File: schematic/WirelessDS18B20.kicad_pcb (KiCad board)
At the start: 2 copper layers, 25.4 x 30.5 mm, 14 parts, among them P1 Power Connector, P2 1-Wire Bus, P3 SERIAL_TX, Q1 BS170, SW1 RESCUE_MODE, SW2 RESET, U1 AMS1117 3.3, U2 ESP-01

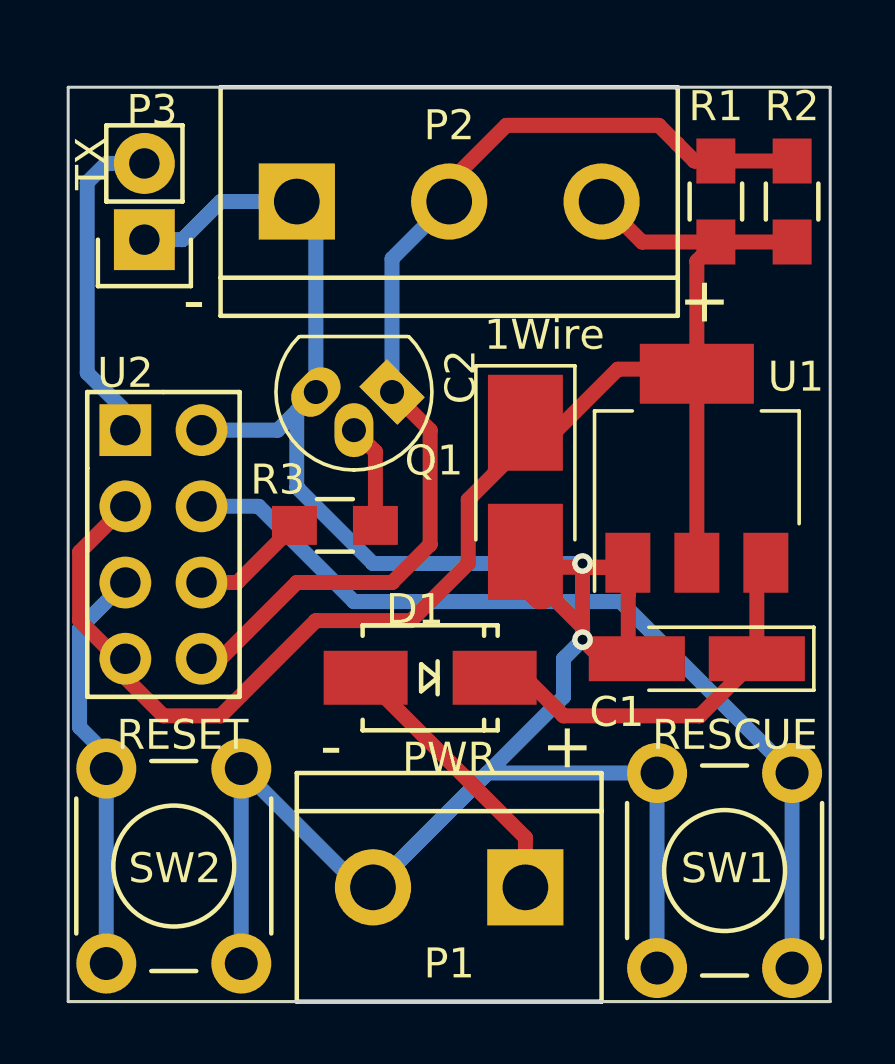
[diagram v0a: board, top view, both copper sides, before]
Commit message: Improve Schematic (update KiCad to 4.0.7)
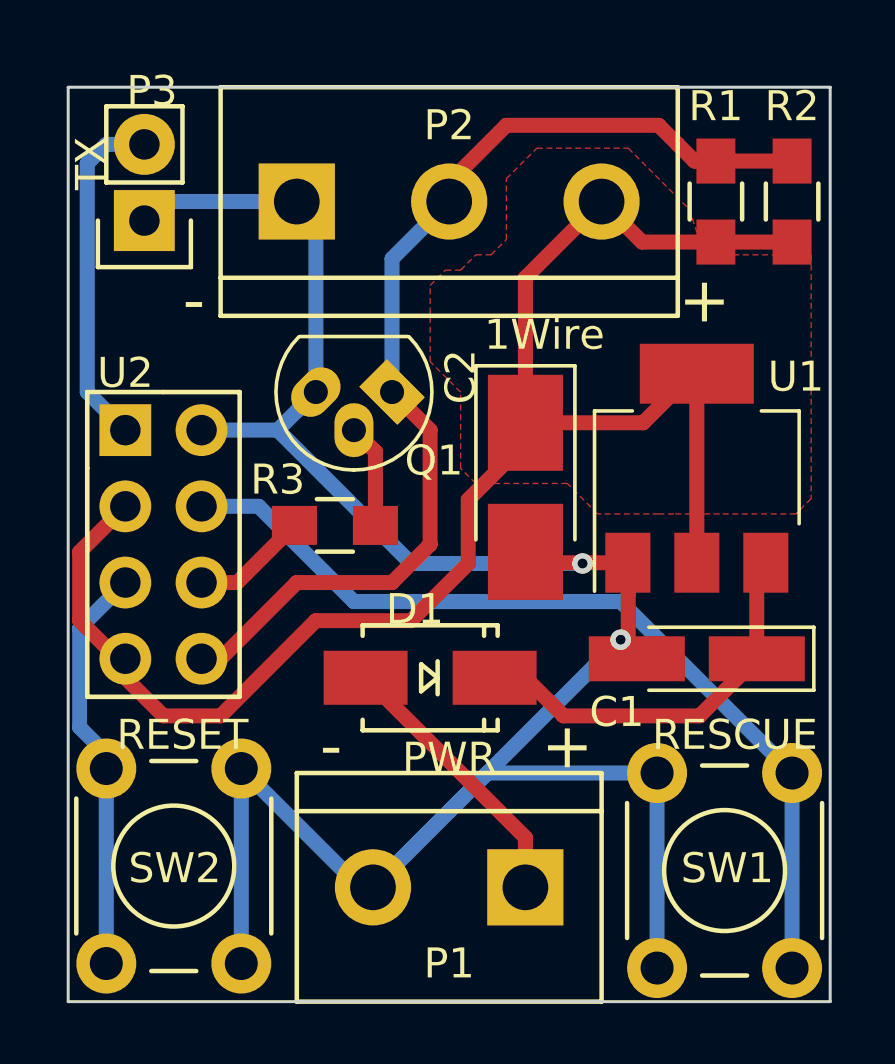
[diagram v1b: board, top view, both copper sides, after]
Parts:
- SW1: value RESCUE_MODE -> SW_Push
- SW2: value RESET -> SW_Push
- U1: value AMS1117 3.3 -> AMS1117-3.3
- moved P3 0.63 mm to (121.3, 69.2)
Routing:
- net GND: track 91.3 -> 81.0 mm
- net VCC: track 51.0 -> 54.6 mm
- net Net-(P3-Pad2): track 10.9 -> 11.6 mm
- added copper zone on F.Cu, net VCC
